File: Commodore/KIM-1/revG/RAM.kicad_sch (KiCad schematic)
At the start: 14 parts

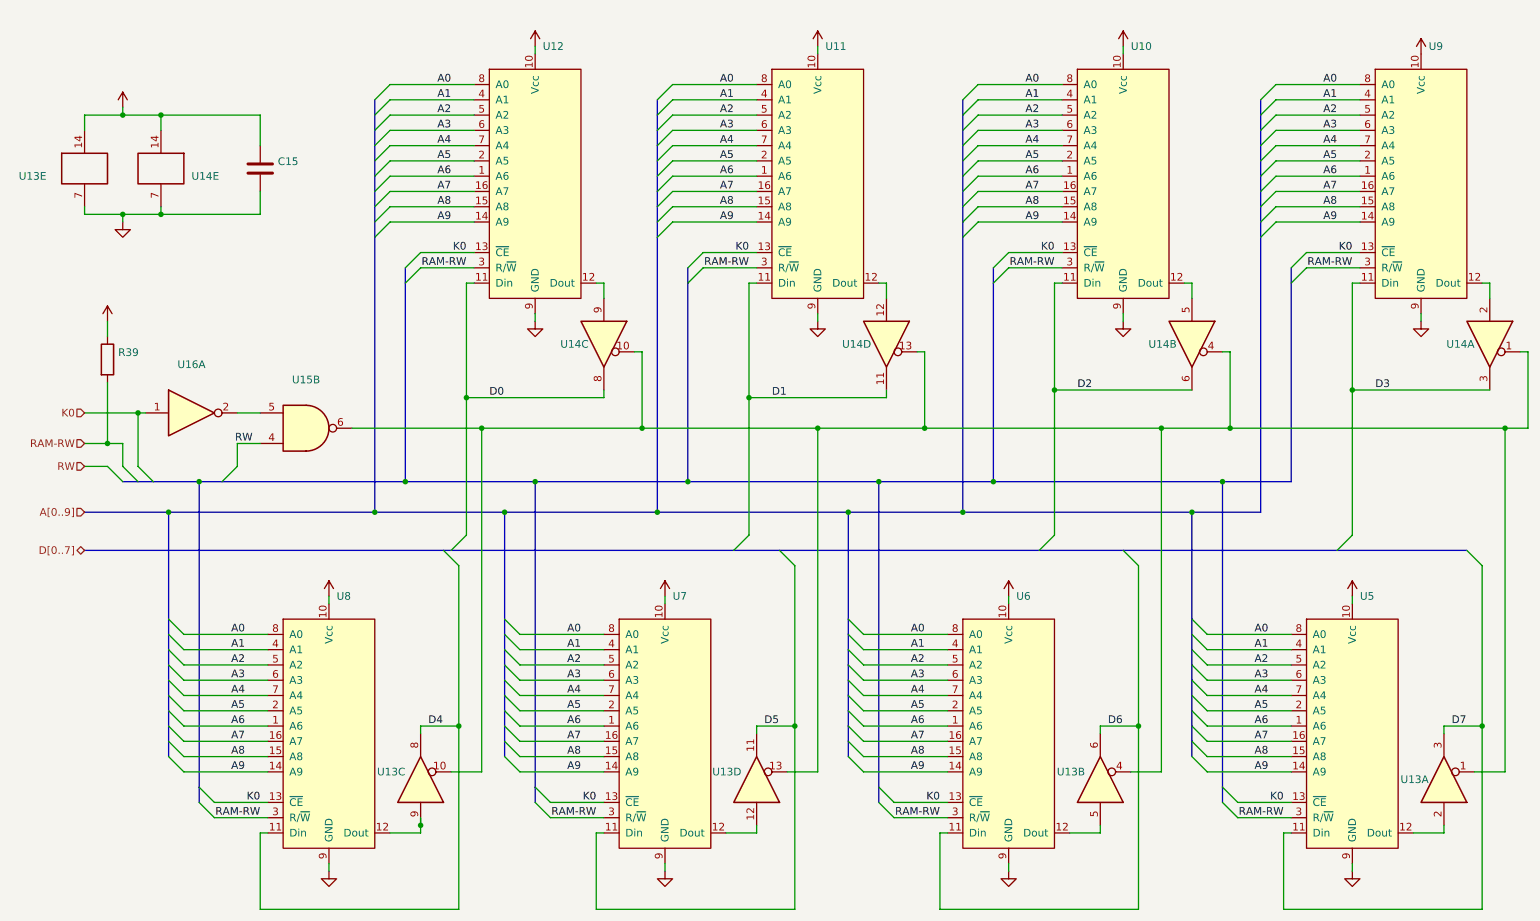
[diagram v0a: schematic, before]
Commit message: Corrected resistor values for R18..R23 and R41..R46 (transposed).
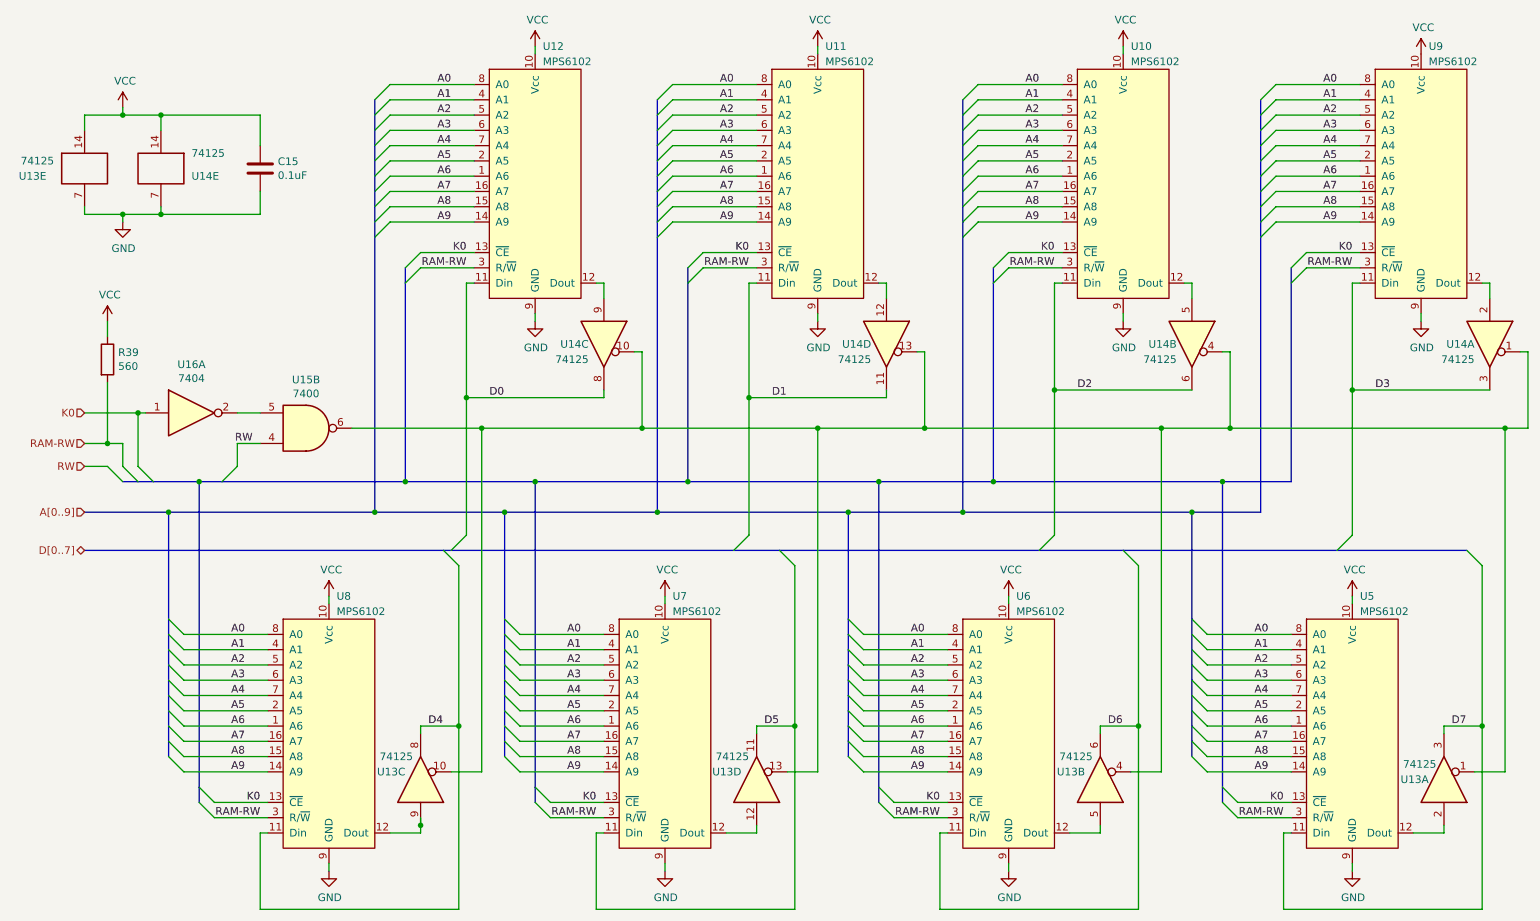
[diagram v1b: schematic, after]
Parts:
- C15: value (none) -> 0.1uF
- R39: value (none) -> 560
- U10, U11, U12, U5, U6, U7, U8, U9: value (none) -> MPS6102
- U13, U14: value (none) -> 74125
- U15: value (none) -> 7400
- U16: value (none) -> 7404
